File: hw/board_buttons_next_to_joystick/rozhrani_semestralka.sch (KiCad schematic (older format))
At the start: 58 parts, among them P1 DISPLAY_CONN, P2 DISPLAY_VCC_CON, P3 USB_B, U1 MCP2210, U2 MIC5504-3.3, U3 Joystick, U4 LM239, U5 CD4532, U6 NPIC6C596, U7 NE555, U8 PB6149L, U9 PB6149L

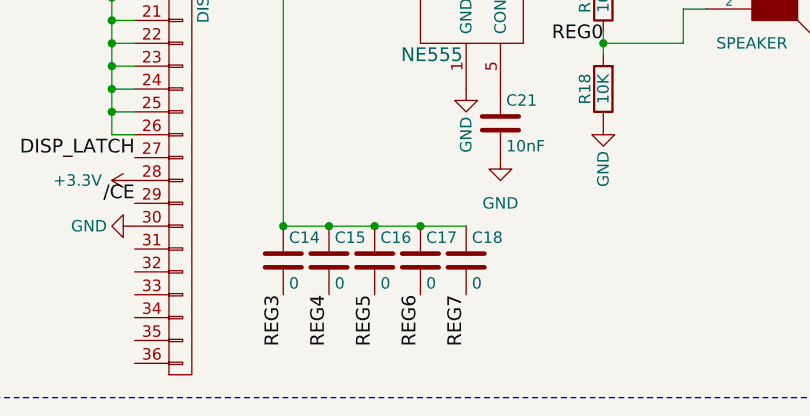
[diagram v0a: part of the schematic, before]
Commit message: added capacitor value to buzzer
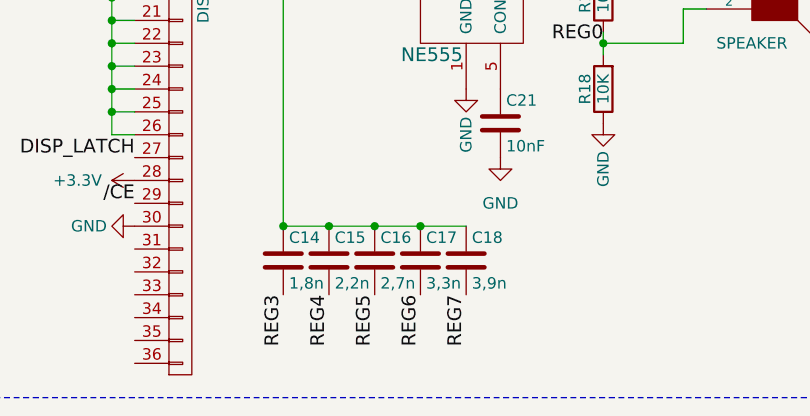
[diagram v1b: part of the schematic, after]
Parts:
- C14: value 0 -> 1,8n
- C15: value 0 -> 2,2n
- C16: value 0 -> 2,7n
- C17: value 0 -> 3,3n
- C18: value 0 -> 3,9n
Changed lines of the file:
@@
 P 3250 7050
 F 0 "C15" H 3275 7150 50  0000 L CNN
-F 1 "0" H 3275 6950 50  0000 L CNN
+F 1 "2,2n" H 3275 6950 50  0000 L CNN
 F 2 "Capacitors_SMD:C_0603_HandSoldering" H 3288 6900 30  0001 C CNN
 F 3 "" H 3250 7050 60  0000 C CNN
@@
 P 3450 7050
 F 0 "C16" H 3475 7150 50  0000 L CNN
-F 1 "0" H 3475 6950 50  0000 L CNN
+F 1 "2,7n" H 3475 6950 50  0000 L CNN
 F 2 "Capacitors_SMD:C_0603_HandSoldering" H 3488 6900 30  0001 C CNN
 F 3 "" H 3450 7050 60  0000 C CNN
@@
 P 3650 7050
 F 0 "C17" H 3675 7150 50  0000 L CNN
-F 1 "0" H 3675 6950 50  0000 L CNN
+F 1 "3,3n" H 3675 6950 50  0000 L CNN
 F 2 "Capacitors_SMD:C_0603_HandSoldering" H 3688 6900 30  0001 C CNN
 F 3 "" H 3650 7050 60  0000 C CNN
@@
 P 3850 7050
 F 0 "C18" H 3875 7150 50  0000 L CNN
-F 1 "0" H 3875 6950 50  0000 L CNN
+F 1 "3,9n" H 3875 6950 50  0000 L CNN
 F 2 "Capacitors_SMD:C_0603_HandSoldering" H 3888 6900 30  0001 C CNN
 F 3 "" H 3850 7050 60  0000 C CNN
@@
 P 3050 7050
 F 0 "C14" H 3075 7150 50  0000 L CNN
-F 1 "0" H 3075 6950 50  0000 L CNN
+F 1 "1,8n" H 3075 6950 50  0000 L CNN
 F 2 "Capacitors_SMD:C_0603_HandSoldering" H 3088 6900 30  0001 C CNN
 F 3 "" H 3050 7050 60  0000 C CNN
